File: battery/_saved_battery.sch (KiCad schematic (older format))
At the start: 40 parts, among them J1 batt_1, J2 batt_2, J3 batt_3, J4 batt_4, J5 reed_switch, J6 toPcb+, J7 toPcb-, J8 on_signal, Q1 batt1_sw, Q2 batt2_sw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

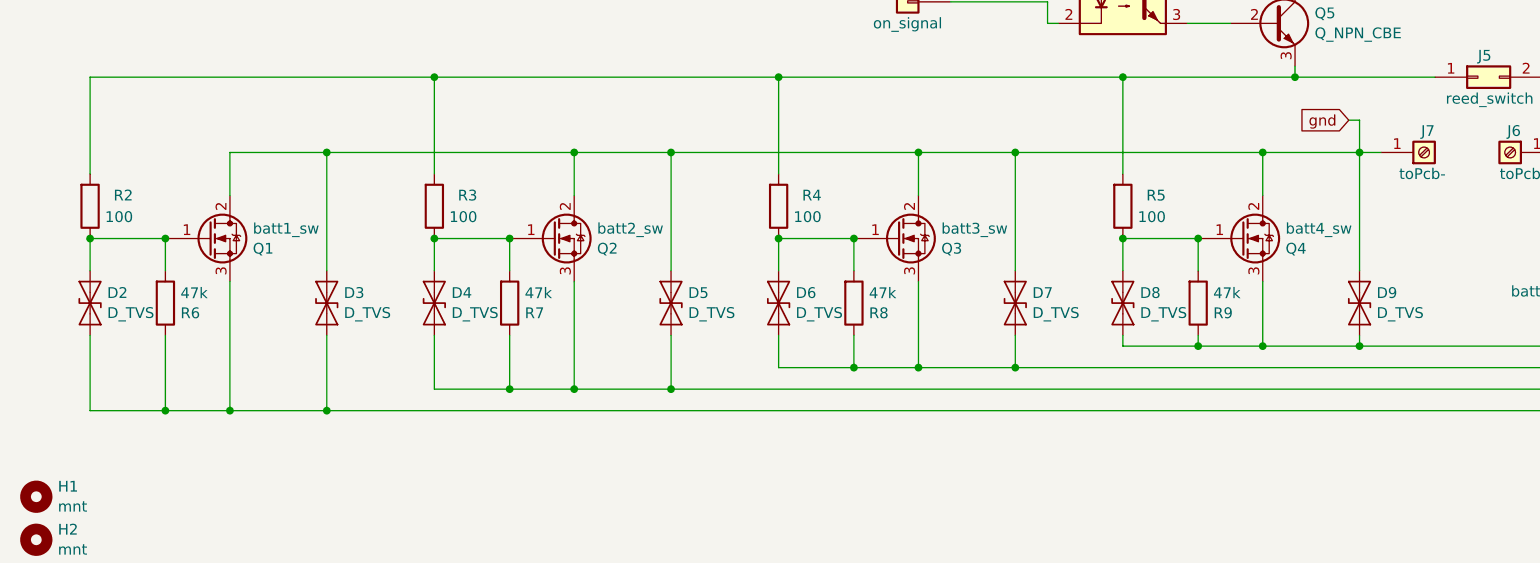
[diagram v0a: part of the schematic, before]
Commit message: capacitor bybpas
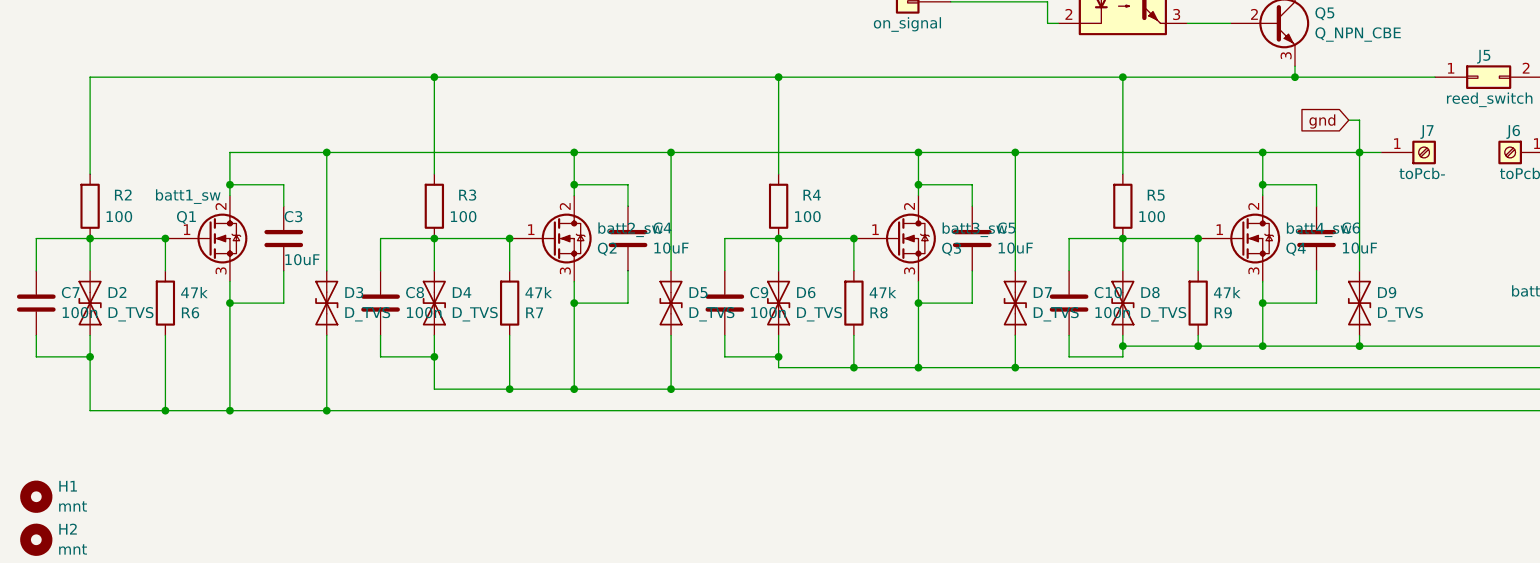
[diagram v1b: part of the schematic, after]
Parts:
- added C10, C7, C8, C9: 100n, Capacitor_SMD:C_0805_2012Metric_Pad1.15x1.40mm_HandSolder, symbol Device:C
- added C3, C4, C5, C6: 10uF, Capacitor_SMD:C_0805_2012Metric_Pad1.15x1.40mm_HandSolder, symbol Device:C
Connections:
- net gnd: now also C3.1, C4.1, C5.1, C6.1
- net at D2.1 (A1), Q1.1 (G), R2.1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: now also C7.2
- net at D2.2 (A2), D3.2 (A2), J1.2 (Pin_2)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: now also C3.2, C7.1
- net at D4.2 (A2), D5.2 (A2), J2.2 (Pin_2)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: now also C4.2, C8.1
- net at D6.2 (A2), D7.2 (A2), J3.2 (Pin_2)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: now also C5.2, C9.1
- net at D8.2 (A2), D9.2 (A2), J4.2 (Pin_2)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: now also C10.1, C6.2
- net at D4.1 (A1), Q2.1 (G), R3.1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: now also C8.2
- net at D6.1 (A1), Q3.1 (G), R4.1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: now also C9.2
- net at D8.1 (A1), Q4.1 (G), R5.1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: now also C10.2
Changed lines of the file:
@@
 U 1 1 5CF2C58F
 P 3000 3150
-F 0 "Q1" H 3206 3103 50  0000 L CNN
-F 1 "batt1_sw" H 3206 3196 50  0000 L CNN
+F 0 "Q1" H 2850 3250 50  0000 L CNN
+F 1 "batt1_sw" H 2750 3350 50  0000 L CNN
 F 2 "Package_TO_SOT_SMD:TO-252-2" H 3200 3250 50  0001 C CNN
 F 3 "~" H 3000 3150 50  0001 C CNN
@@
 Wire Wire Line
 	6300 3750 6750 3750
-Wire Wire Line
-	7900 3350 7900 3650
 Connection ~ 7900 3650
 Wire Wire Line
@@
 Connection ~ 7250 3150
 Wire Wire Line
-	3100 2750 3100 2950
+	3100 2750 3100 2900
 Wire Wire Line
 	3550 2750 3550 3300
 Connection ~ 3550 2750
-Wire Wire Line
-	3550 2750 3100 2750
-Wire Wire Line
-	4700 2750 4700 2950
 Connection ~ 4700 2750
 Wire Wire Line
@@
 Wire Wire Line
 	5150 2750 4700 2750
-Wire Wire Line
-	6300 2750 6300 2950
 Connection ~ 6300 2750
 Wire Wire Line
@@
 Wire Wire Line
 	6750 2750 6300 2750
-Wire Wire Line
-	7900 2750 7900 2950
 Connection ~ 7900 2750
 Wire Wire Line
@@
 Wire Wire Line
 	2450 3950 2800 3950
-Wire Wire Line
-	2450 3600 2450 3950
 Wire Wire Line
 	2800 3600 2800 3950
@@
 	2800 3950 3100 3950
 Wire Wire Line
-	3100 3350 3100 3950
+	3100 3350 3100 3450
 Wire Wire Line
 	3550 3600 3550 3950
 Wire Wire Line
-	4050 3600 4050 3850
-Wire Wire Line
 	4400 3600 4400 3850
 Wire Wire Line
-	4700 3350 4700 3850
-Wire Wire Line
 	5150 3600 5150 3850
 Wire Wire Line
-	5650 3600 5650 3750
-Wire Wire Line
 	6000 3600 6000 3750
-Wire Wire Line
-	6300 3350 6300 3750
 Wire Wire Line
 	6750 3600 6750 3750
@@
 Wire Wire Line
 	7250 2850 7250 2400
-Connection ~ 7250 2400
-Wire Wire Line
-	7250 2400 8050 2400
 Wire Wire Line
 	5650 2850 5650 2400
@@
 Wire Wire Line
 	8050 2350 8050 2400
-Connection ~ 8050 2400
 Wire Wire Line
 	8050 2400 8700 2400
@@
 	1    0    0    -1
 $EndComp
+$Comp
+L Device:C C3
+U 1 1 5D1B82C7
+P 3350 3150
+F 0 "C3" H 3350 3250 50  0000 L CNN
+F 1 "10uF" H 3350 3050 50  0000 L CNN
+F 2 "Capacitor_SMD:C_0805_2012Metric_Pad1.15x1.40mm_HandSolder" H 3388 3000 50  0001 C CNN
+F 3 "~" H 3350 3150 50  0001 C CNN
+	1    3350 3150
+	1    0    0    -1
+$EndComp
+Wire Wire Line
+	3350 3300 3350 3450
+Wire Wire Line
+	3350 3450 3100 3450
+Connection ~ 3100 3450
+Wire Wire Line
+	3100 3450 3100 3950
+Wire Wire Line
+	3100 2750 3550 2750
+Wire Wire Line
+	3350 3000 3350 2900
+Wire Wire Line
+	3350 2900 3100 2900
+Connection ~ 3100 2900
+Wire Wire Line
+	3100 2900 3100 2950
+$Comp
+L Device:C C4
+U 1 1 5D1CD1AE
+P 4950 3150
+F 0 "C4" H 5065 3197 50  0000 L CNN
+F 1 "10uF" H 5065 3104 50  0000 L CNN
+F 2 "Capacitor_SMD:C_0805_2012Metric_Pad1.15x1.40mm_HandSolder" H 4988 3000 50  0001 C CNN
+F 3 "~" H 4950 3150 50  0001 C CNN
+	1    4950 3150
+	1    0    0    -1
+$EndComp
+Wire Wire Line
+	4950 3300 4950 3450
+Wire Wire Line
+	4950 3450 4700 3450
+Wire Wire Line
+	4950 3000 4950 2900
+Wire Wire Line
+	4950 2900 4700 2900
+$Comp
+L Device:C C5
+U 1 1 5D1D0F67
+P 6550 3150
+F 0 "C5" H 6665 3197 50  0000 L CNN
+F 1 "10uF" H 6665 3104 50  0000 L CNN
+F 2 "Capacitor_SMD:C_0805_2012Metric_Pad1.15x1.40mm_HandSolder" H 6588 3000 50  0001 C CNN
+F 3 "~" H 6550 3150 50  0001 C CNN
+	1    6550 3150
+	1    0    0    -1
+$EndComp
+Wire Wire Line
+	6550 3300 6550 3450
+Wire Wire Line
+	6550 3450 6300 3450
+Wire Wire Line
+	6550 3000 6550 2900
+Wire Wire Line
+	6550 2900 6300 2900
+$Comp
+L Device:C C6
+U 1 1 5D1D97C7
+P 8150 3150
+F 0 "C6" H 8265 3197 50  0000 L CNN
+F 1 "10uF" H 8265 3104 50  0000 L CNN
+F 2 "Capacitor_SMD:C_0805_2012Metric_Pad1.15x1.40mm_HandSolder" H 8188 3000 50  0001 C CNN
+F 3 "~" H 8150 3150 50  0001 C CNN
+	1    8150 3150
+	1    0    0    -1
+$EndComp
+Wire Wire Line
+	8150 3300 8150 3450
+Wire Wire Line
+	8150 3450 7900 3450
+Wire Wire Line
+	8150 3000 8150 2900
+Wire Wire Line
+	8150 2900 7900 2900
+Wire Wire Line
+	4700 2750 4700 2900
+Connection ~ 4700 2900
+Wire Wire Line
+	4700 2900 4700 2950
+Wire Wire Line
+	4700 3350 4700 3450
+Connection ~ 4700 3450
+Wire Wire Line
+	4700 3450 4700 3850
+Wire Wire Line
+	6300 3350 6300 3450
+Connection ~ 6300 3450
+Wire Wire Line
+	6300 3450 6300 3750
+Wire Wire Line
+	6300 2750 6300 2900
+Connection ~ 6300 2900
+Wire Wire Line
+	6300 2900 6300 2950
+Wire Wire Line
+	7900 2750 7900 2900
+Connection ~ 7900 2900
+Wire Wire Line
+	7900 2900 7900 2950
+Wire Wire Line
+	7900 3350 7900 3450
+Connection ~ 7900 3450
+Wire Wire Line
+	7900 3450 7900 3650
+Wire Wire Line
+	7250 2400 8050 2400
+Connection ~ 7250 2400
+Connection ~ 8050 2400
+$Comp
+L Device:C C7
+U 1 1 5D247DA5
+P 2200 3450
+F 0 "C7" H 2085 3403 50  0000 R CNN
+F 1 "100n" H 2085 3496 50  0000 R CNN
+F 2 "Capacitor_SMD:C_0805_2012Metric_Pad1.15x1.40mm_HandSolder" H 2238 3300 50  0001 C CNN
+F 3 "~" H 2200 3450 50  0001 C CNN
+	1    2200 3450
+	-1   0    0    1
+$EndComp
+Wire Wire Line
+	2200 3300 2200 3150
+Wire Wire Line
+	2200 3150 2450 3150
+Wire Wire Line
+	2200 3600 2200 3700
+Wire Wire Line
+	2200 3700 2450 3700
+$Comp
+L Device:C C8
+U 1 1 5D24D386
+P 3800 3450
+F 0 "C8" H 3685 3403 50  0000 R CNN
+F 1 "100n" H 3685 3496 50  0000 R CNN
+F 2 "Capacitor_SMD:C_0805_2012Metric_Pad1.15x1.40mm_HandSolder" H 3838 3300 50  0001 C CNN
+F 3 "~" H 3800 3450 50  0001 C CNN
+	1    3800 3450
+	-1   0    0    1
+$EndComp
+Wire Wire Line
+	3800 3300 3800 3150
+Wire Wire Line
+	3800 3150 4050 3150
+Wire Wire Line
+	3800 3600 3800 3700
+Wire Wire Line
+	3800 3700 4050 3700
+$Comp
+L Device:C C9
+U 1 1 5D252E37
+P 5400 3450
+F 0 "C9" H 5285 3403 50  0000 R CNN
+F 1 "100n" H 5285 3496 50  0000 R CNN
+F 2 "Capacitor_SMD:C_0805_2012Metric_Pad1.15x1.40mm_HandSolder" H 5438 3300 50  0001 C CNN
+F 3 "~" H 5400 3450 50  0001 C CNN
+	1    5400 3450
+	-1   0    0    1
+$EndComp
+Wire Wire Line
+	5400 3300 5400 3150
+Wire Wire Line
+	5400 3150 5650 3150
+Wire Wire Line
+	5400 3600 5400 3700
+Wire Wire Line
+	5400 3700 5650 3700
+$Comp
+L Device:C C10
+U 1 1 5D258E5B
+P 7000 3450
+F 0 "C10" H 6885 3403 50  0000 R CNN
+F 1 "100n" H 6885 3496 50  0000 R CNN
+F 2 "Capacitor_SMD:C_0805_2012Metric_Pad1.15x1.40mm_HandSolder" H 7038 3300 50  0001 C CNN
+F 3 "~" H 7000 3450 50  0001 C CNN
+	1    7000 3450
+	-1   0    0    1
+$EndComp
+Wire Wire Line
+	7000 3300 7000 3150
+Wire Wire Line
+	7000 3150 7250 3150
+Wire Wire Line
+	7000 3600 7000 3700
+Wire Wire Line
+	7000 3700 7250 3700
+Wire Wire Line
+	2450 3600 2450 3700
+Connection ~ 2450 3700
+Wire Wire Line
+	2450 3700 2450 3950
+Wire Wire Line
+	4050 3600 4050 3700
+Connection ~ 4050 3700
+Wire Wire Line
+	4050 3700 4050 3850
+Wire Wire Line
+	5650 3600 5650 3700
+Connection ~ 5650 3700
+Wire Wire Line
+	5650 3700 5650 3750
+Wire Wire Line
+	7250 3700 7250 3650
+Connection ~ 7250 3650
 $EndSCHEMATC
